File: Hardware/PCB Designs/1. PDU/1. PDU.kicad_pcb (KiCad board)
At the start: 4 copper layers, 150.5 x 116.5 mm, 110 parts, among them J1 XT60-M, J2 Conn_01x02_Pin, J3 Conn_01x02_Pin, J4 To MCU, J5 To Communication Card, J6 Conn_01x03_Pin, J7 Conn_01x08_Pin, K1 SRD-05VDC-SL-C, Q1 BC547, SW1 SW_Push, U10 LM2596S-3.3, U11 PC817, U12 PC817, U13 PC817, U14 MAX481E, U15 AP2112K-3.3, U16 LM2596S-5, U2 TP5100, U3 MT3608, U4 PC817, U5 PC817, U6 ATmega8-16A, U8 TPS2116DRL, U9 TPS2116DRL, Y1 Crystal

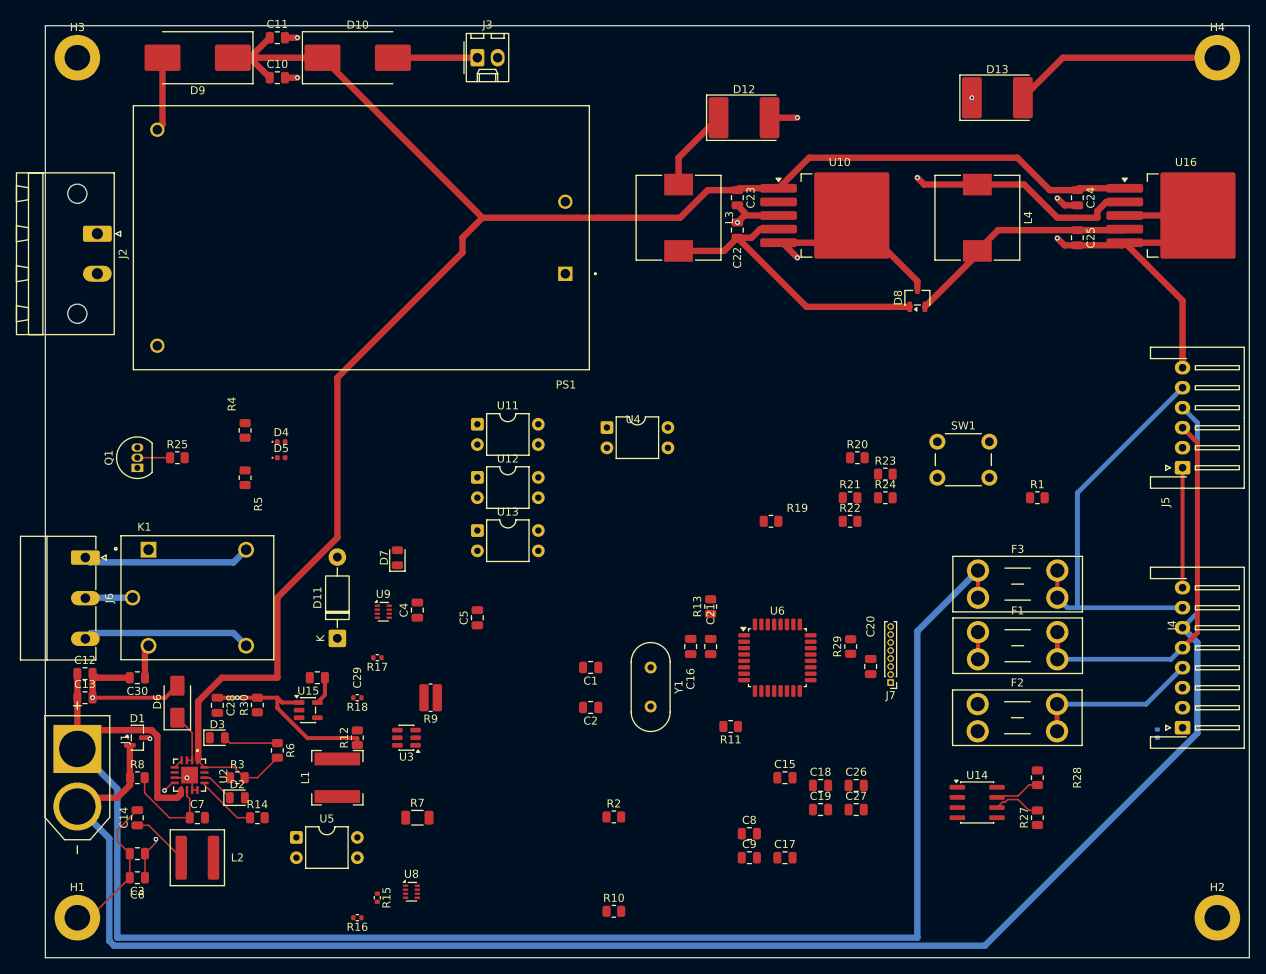
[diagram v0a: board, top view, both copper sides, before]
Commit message: Update docs/index.md with new assets
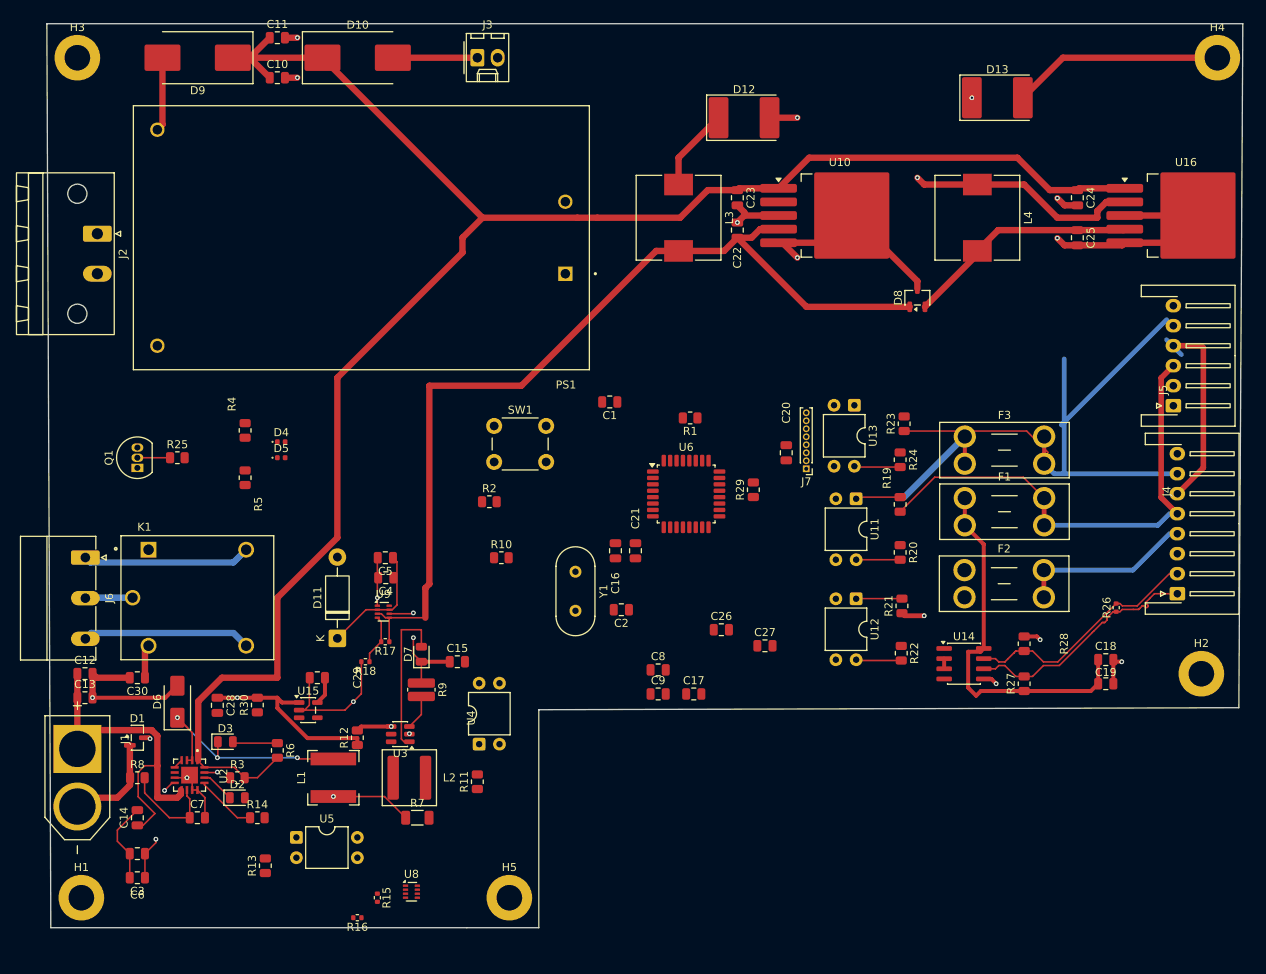
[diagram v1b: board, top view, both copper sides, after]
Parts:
- added H5: MountingHole_Pad, MountingHole:MountingHole_3.2mm_M3_ISO7380_Pad, F.Cu at (89.0, 135.0)
- R26: moved to F.Cu
- moved R13 64.4 mm to (58.5, 131.0)
- moved SW1 55.4 mm to (87.1, 76.0)
- moved U12 49.7 mm to (132.3, 97.6), turned to -90 degrees
- moved U13 49.7 mm to (132.1, 73.4), turned to -90 degrees
- moved U11 48.3 mm to (132.3, 85.1), turned to -90 degrees
- moved R10 46.4 mm to (88.0, 92.5)
- moved R1 44.5 mm to (111.6, 75.0), turned to 180 degrees
- moved C15 43.4 mm to (82.5, 105.5)
- moved U4 42.7 mm to (85.2, 115.8), turned to 90 degrees
- moved R2 42.4 mm to (86.5, 85.5)
- moved C18 39.0 mm to (163.6, 105.2)
- moved C19 39.0 mm to (163.6, 108.2)
- moved C1 33.3 mm to (101.5, 73.0)
- moved R11 32.4 mm to (85.0, 120.5), turned to 90 degrees
- moved H2 30.6 mm to (175.5, 107.0)
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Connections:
- J4 pad 1: RS458R- -> RS458R+
- J4 pad 2: RS458R+ -> RS458R-
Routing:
- net BATT_NEG: track 221.4 -> 38.7 mm
- net BAT_OUT_DIR: track 264.2 -> 104.6 mm
- net 5V_ACTIVE_SOURCE: track 38.8 -> 115.3 mm
- net +5V: track 33.8 -> 92.3 mm
- net Net-(J4-Pin_4): track 21.0 -> 59.8 mm, vias 0 -> 1
- net Net-(U2-VS): track 13.6 -> 45.1 mm, vias 2 -> 3
- net RS458R-: track 5.69 -> 29.3 mm
- net RS458R+: track 6.03 -> 29.3 mm
- net Net-(D6-K): track 8.43 -> 30.1 mm, vias 0 -> 2
- net Net-(D7-A): track 0.00 -> 19.4 mm
- net Net-(J4-Pin_7): track 52.5 -> 71.6 mm
- net Net-(U3-EN): track 0.00 -> 17.7 mm, vias 0 -> 1
- net MT3608_OUT: track 0.00 -> 15.8 mm, vias 0 -> 2
- net Net-(J4-Pin_5): track 48.7 -> 60.5 mm
- net Net-(D11-A): track 26.1 -> 36.9 mm
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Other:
- board size 150.5 x 116.5 mm -> 149.5 x 113 mm
